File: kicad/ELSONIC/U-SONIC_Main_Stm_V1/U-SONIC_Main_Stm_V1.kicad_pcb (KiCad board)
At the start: 2 copper layers, 200 x 150 mm, 193 parts, among them IC1 LM5005MHX_NOPB, J1 SMW250-02P, J2 Screw_Terminal_01x06, J3 ARM_SWD_10, J4 Conn_01x06_HEADERPIN, J5 Conn_01x03, J6 Conn_02x10_Odd_Even, J7 SMW250-02P, J8 Conn_02x13_Odd_Even, K1 G6A274, K2 PA1A_5V, K3 PA1A_5V, K4 G6A274, K5 PA1A_5V, K6 G6A274, K7 PA1A_5V, K8 PA1A_5V, K9 G6A274, Q1 STD25N10F7, Q2 STD25N10F7, SW1 TS-1088, SW2 DSHP02T, T1 TOROID_OUTPUT_OD20_T6T12, T2 TOROID_CT_OD16_T1T20, U1 AMS1117-3.3, U10 TLP185GB-S, U11 TLP185GB-S, U12 TLP185GB-S, U2 UCC21520DWR, U3 STM32G474RBT6, U4 INA190A3IDCKR, U5 MAX3485ESA, U6 TLP185GB-S, U7 ULN2003ADR, U8 ULN2003ADR, U9 TLP185GB-S, Y1 X49SM8M

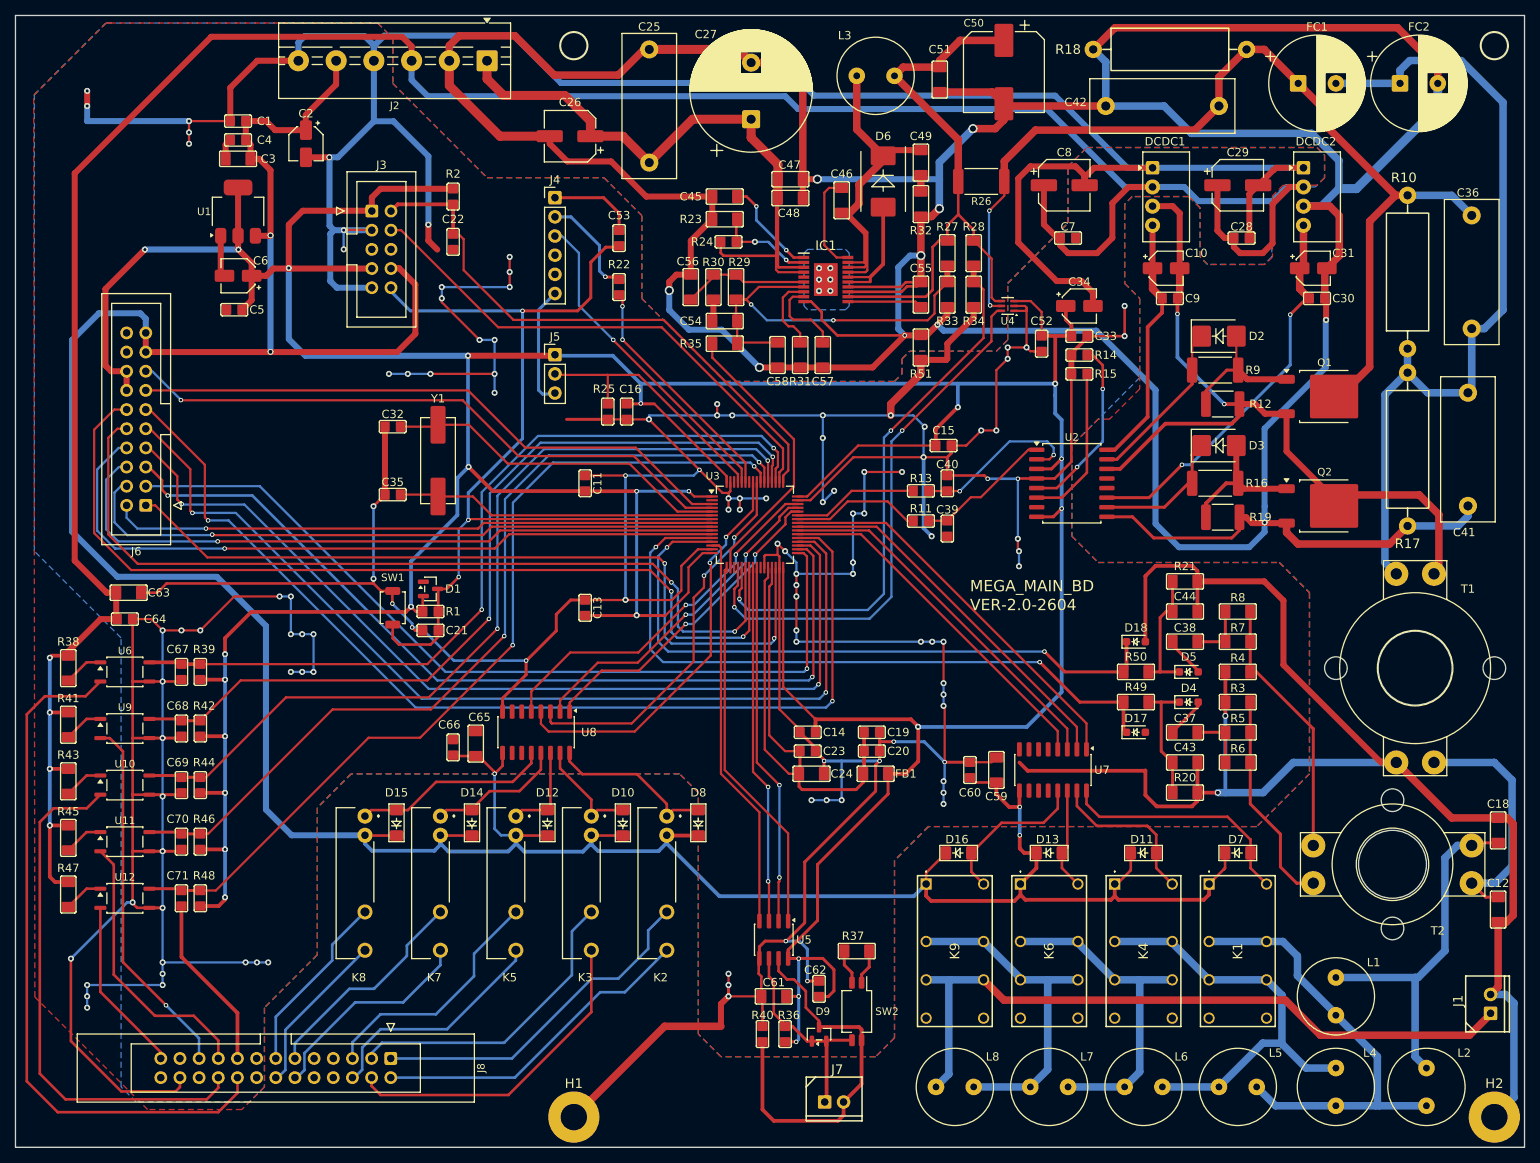
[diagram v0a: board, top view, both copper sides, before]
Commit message: feat: update ultrasonic controller and board design
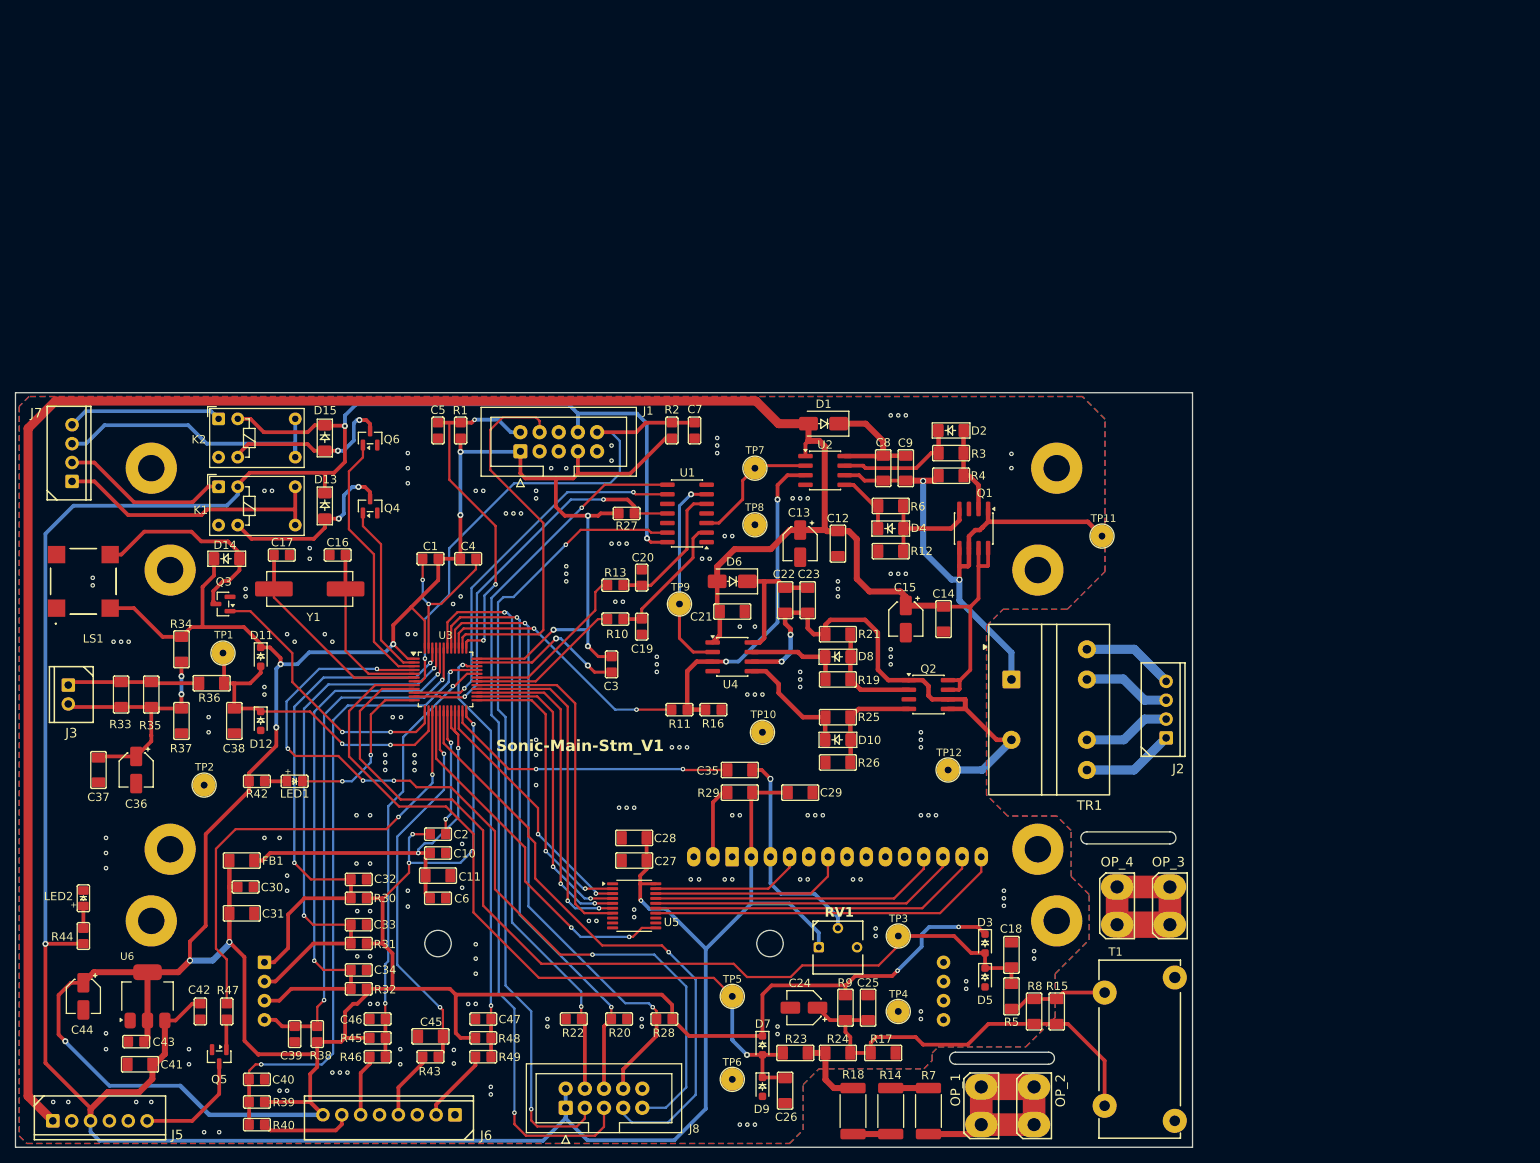
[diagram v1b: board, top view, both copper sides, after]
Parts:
- removed C48: CL31B225K, 04_MyFoot_Passive:C_3216Metric
- removed C49, C57: 1206CG331J101NT, 04_MyFoot_Passive:C_3216Metric
- removed C50: 220UF50V67RV, 04_MyFoot_Passive:CP_Elec_10x10.5
- removed C51: CL31A106K, 04_MyFoot_Passive:C_3216Metric
- removed C52, C53, C60, C62, C64, C66: CL21B104K, 04_MyFoot_Passive:C_2012Metric
- removed C54, C58: 1206B103K, 04_MyFoot_Passive:C_3216Metric
- removed C55: 1206CG102J101NT, 04_MyFoot_Passive:C_3216Metric
- removed C56: 1206CG101J, 04_MyFoot_Passive:C_3216Metric
- removed C59, C65: CL31B106K, 04_MyFoot_Passive:C_3216Metric
- removed C61, C63: CL31B105K, 04_MyFoot_Passive:C_3216Metric
- removed C67, C68, C69, C70, C71: CL21B472K, 04_MyFoot_Passive:C_2012Metric
- removed D16: LL4148, 03_MyFoot_Active:LL4148_MELF
- removed D17, D18: MM3Z3V6, 03_MyFoot_Active:D_SOD-323_HandSoldering
- removed DCDC1, DCDC2: MUS2415N, 05_MyFoot_Others:MUS2415N
- removed FC1, FC2: 470UF63V, 04_MyFoot_Passive:CP_Radial_D12.5mm_P5.00mm
- removed IC1: LM5005MHX_NOPB, 01_MyFoot_ICs:SOP65P640X110-21N
- removed K3, K5, K7, K8: PA1A_5V, 06_MyFoot_Mechanical:PA1A5V
- removed K4, K6, K9: G6A274, 06_MyFoot_Mechanical:G6A274PST15USDC12
- removed L1: 3.3uH, 04_MyFoot_Passive:L_Radial_D10.0mm_P5.00mm
- removed L2: 3.9uH, 04_MyFoot_Passive:L_Radial_D10.0mm_P5.00mm
- removed L3: 33uH, 04_MyFoot_Passive:L_Radial_D10.0mm_P5.00mm
- removed L4: 1.5uH, 04_MyFoot_Passive:L_Radial_D10.0mm_P5.00mm
- removed L5: 2.2uH, 04_MyFoot_Passive:L_Radial_D10.0mm_P5.00mm
- removed L6: 2.7uH, 04_MyFoot_Passive:L_Radial_D10.0mm_P5.00mm
- removed L7: 4.7uH, 04_MyFoot_Passive:L_Radial_D10.0mm_P5.00mm
- removed L8: 6.8uH, 04_MyFoot_Passive:L_Radial_D10.0mm_P5.00mm
- removed R41: W4J0472, 04_MyFoot_Passive:R_3216Metric
- removed R50: W4J0102, 04_MyFoot_Passive:R_3216Metric
- removed R51: W4F0000, 04_MyFoot_Passive:R_3216Metric
- removed SW1: TS-1088, 06_MyFoot_Mechanical:SW_SPST_TS-1088-xR025
- removed SW2: DSHP02T, 06_MyFoot_Mechanical:CHS-02B_W7.62mm_P1.27mm
- removed T2: TOROID_CT_OD16_T1T20, 04_MyFoot_Passive:Toroid_OD16mm_ID9.6-T1T20
- removed U10, U11, U12, U9: TLP185GB-S, 01_MyFoot_ICs:SOIC-4_4.55x3.7mm_P2.54mm
- removed U7, U8: ULN2003ADR, 01_MyFoot_ICs:SOIC-16_3.9x9.9mm_P1.27mm
- added C17: CG330J, 04_MyFoot_Passive:C_2012Metric, F.Cu at (35.3, -78.5)
- added LCD1: LC1622, 06_MyFoot_Mechanical:LC1622_1, B.Cu at (78.0, -60.0)
- added LED1: LED_SMD_KT_0805R, 03_MyFoot_Active:LED_2012Metric, F.Cu at (37.0, -48.5)
- added LED2: LED_SMD_KT_0805R, 03_MyFoot_Active:LED_2012Metric, F.Cu at (9.00, -33.0)
- added LS1: MLT-8530, 03_MyFoot_Active:MLT8530, F.Cu at (9.00, -75.0)
- added OP_1: TAP_250, 02_MyFoot_Connectors:TAP_250, F.Cu at (128.0, -5.50)
- added OP_2: TAP_250, 02_MyFoot_Connectors:TAP_250, F.Cu at (135.0, -5.50)
- added OP_3: TAP_250, 02_MyFoot_Connectors:TAP_250, F.Cu at (153.0, -32.0)
- added OP_4: TAP_250, 02_MyFoot_Connectors:TAP_250, F.Cu at (146.0, -32.0)
- added Q3: KRC105S, 03_MyFoot_Active:SOT-23_KRC105S, F.Cu at (27.5, -72.0)
- added Q4: KRC105S, 03_MyFoot_Active:SOT-23_KRC105S, F.Cu at (47.0, -85.0)
- added Q5: 2SC5343, 03_MyFoot_Active:SOT-23, F.Cu at (27.0, -12.0)
- added Q6: KRC105S, 03_MyFoot_Active:SOT-23_KRC105S, F.Cu at (47.0, -94.0)
- added RV1: 3362P103, 04_MyFoot_Passive:TRIM_3362P, F.Cu at (109.0, -26.5)
- added TP1: TPOINT, 05_MyFoot_Others:TP, F.Cu at (27.5, -65.5)
- added TP10: TPOINT, 05_MyFoot_Others:TP, F.Cu at (99.0, -55.0)
- added TP11: TPOINT, 05_MyFoot_Others:TP, F.Cu at (144.0, -81.0)
- added TP12: TPOINT, 05_MyFoot_Others:TP, F.Cu at (123.6, -50.0)
- added TP2: TPOINT, 05_MyFoot_Others:TP, F.Cu at (25.0, -48.0)
- added TP3: TPOINT, 05_MyFoot_Others:TP, F.Cu at (117.0, -28.0)
- added TP4: TPOINT, 05_MyFoot_Others:TP, F.Cu at (117.0, -18.0)
- added TP5: TPOINT, 05_MyFoot_Others:TP, F.Cu at (95.0, -20.0)
- added TP6: TPOINT, 05_MyFoot_Others:TP, F.Cu at (95.0, -9.00)
- added TP7: TPOINT, 05_MyFoot_Others:TP, F.Cu at (98.0, -90.0)
- added TP8: TPOINT, 05_MyFoot_Others:TP, F.Cu at (98.0, -82.5)
- added TP9: TPOINT, 05_MyFoot_Others:TP, F.Cu at (88.0, -72.0)
- added TR1: EI2218, 04_MyFoot_Passive:EI2218, F.Cu at (137.0, -58.0)
- C10, C2, C34, C6: value 10UF25V67RV -> CL21B104K; footprint 04_MyFoot_Passive:CP_Elec_4x5.4 -> 04_MyFoot_Passive:C_2012Metric
- C11, C28: value CL21B104K -> CL31B475K; footprint 04_MyFoot_Passive:C_2012Metric -> 04_MyFoot_Passive:C_3216Metric
- C12: value CG100J -> CL31B105K
- C13, C15: value CL21B104K -> 10UF25V67RV; footprint 04_MyFoot_Passive:C_2012Metric -> 04_MyFoot_Passive:CP_Elec_4x5.4
- C14, C21: value CL21B104K -> CL31B105K; footprint 04_MyFoot_Passive:C_2012Metric -> 04_MyFoot_Passive:C_3216Metric
- C16: value CL21B104K -> CG330J
- C18: value CG100J -> 22pF
- C19: value CL21B104K -> CG220J
- C20: value CL21B475K -> CG220J
- C22: value CL21C101J -> CL31B105K; footprint 04_MyFoot_Passive:C_2012Metric -> 04_MyFoot_Passive:C_3216Metric
- C23, C9: value CL21B104K -> CL31B104K; footprint 04_MyFoot_Passive:C_2012Metric -> 04_MyFoot_Passive:C_3216Metric
- C24: value CL31B106K -> 10UF25V67RV; footprint 04_MyFoot_Passive:C_3216Metric -> 04_MyFoot_Passive:CP_Elec_4x5.4
- C25: value 0.1uF100V -> CL31B104K; footprint 04_MyFoot_Passive:C_Rect_W7.0mm_P15.00mm -> 04_MyFoot_Passive:C_3216Metric
- C26: value 10UF100V67RV -> 22pF; footprint 04_MyFoot_Passive:CP_Elec_6.3x7.7 -> 04_MyFoot_Passive:C_3216Metric
- C27: value 1000UF63V -> CL31B104K; footprint 04_MyFoot_Passive:CP_Radial_D16.0mm_P7.50mm -> 04_MyFoot_Passive:C_3216Metric
- C29: value 47UF50V67RV -> CL31B104K; footprint 04_MyFoot_Passive:CP_Elec_6.3x7.7 -> 04_MyFoot_Passive:C_3216Metric
- C3: value CL31B106K -> CL21B104K; footprint 04_MyFoot_Passive:C_3216Metric -> 04_MyFoot_Passive:C_2012Metric
- C31: value 10UF25V67RV -> CL31B475K; footprint 04_MyFoot_Passive:CP_Elec_4x5.4 -> 04_MyFoot_Passive:C_3216Metric
- C32: value CG330J -> CL21B104K
- C35: value CG330J -> CL31B104K; footprint 04_MyFoot_Passive:C_2012Metric -> 04_MyFoot_Passive:C_3216Metric
- C36: value 0.1uF100V -> 10UF25V67RV; footprint 04_MyFoot_Passive:C_Rect_W7.0mm_P15.00mm -> 04_MyFoot_Passive:CP_Elec_4x5.4
- C39, C40: value CG220J -> CL21B104K
- C41: value 0.1uF100V -> CL31B106K; footprint 04_MyFoot_Passive:C_Rect_W7.0mm_P15.00mm -> 04_MyFoot_Passive:C_3216Metric
- C42: value 1uF100V -> CL21B104K; footprint 04_MyFoot_Passive:C_Rect_W7.0mm_P15.00mm -> 04_MyFoot_Passive:C_2012Metric
- C43: value CL31B104K -> CL21B104K; footprint 04_MyFoot_Passive:C_3216Metric -> 04_MyFoot_Passive:C_2012Metric
- C44: value CL31B104K -> 10UF25V67RV; footprint 04_MyFoot_Passive:C_3216Metric -> 04_MyFoot_Passive:CP_Elec_4x5.4
- C45: value 1206B105K101NT -> CL31B105K
- C46: value 1206B223K101NT -> CL21B104K; footprint 04_MyFoot_Passive:C_3216Metric -> 04_MyFoot_Passive:C_2012Metric
- C47: value CL31B225K -> CL21B104K; footprint 04_MyFoot_Passive:C_3216Metric -> 04_MyFoot_Passive:C_2012Metric
- C5: value CL21B104K -> CL21C101J
- C8: value 47UF50V67RV -> CL31B105K; footprint 04_MyFoot_Passive:CP_Elec_6.3x7.7 -> 04_MyFoot_Passive:C_3216Metric
- D1: value BAV99 -> UF4007; footprint 03_MyFoot_Active:SOT-23 -> 03_MyFoot_Active:D_SMA
- D11, D12, D7: value LL4148 -> BAT54WSQ-7; footprint 03_MyFoot_Active:LL4148_MELF -> 03_MyFoot_Active:D_SOD-323_HandSoldering
- D2: value SS24B -> LL4148; footprint 03_MyFoot_Active:D_SMB -> 03_MyFoot_Active:LL4148_MELF
- D3: value SS24B -> BAT54WSQ-7; footprint 03_MyFoot_Active:D_SMB -> 03_MyFoot_Active:D_SOD-323_HandSoldering
- D4: value BAT54WSQ-7 -> LL4148; footprint 03_MyFoot_Active:D_SOD-323_HandSoldering -> 03_MyFoot_Active:LL4148_MELF
- D6: value B3100-13-F -> UF4007; footprint 03_MyFoot_Active:B3100_13_F -> 03_MyFoot_Active:D_SMA
- D9: value SM712-LF-T7 -> BAT54WSQ-7; footprint Package_TO_SOT_SMD:SOT-23 -> 03_MyFoot_Active:D_SOD-323_HandSoldering
- H3, H4: value MountingHole -> MountingHole_Pad; footprint 06_MyFoot_Mechanical:MTHole_3.5mm -> 06_MyFoot_Mechanical:MTHole_3.5mm_6.8mmPad_GND
- J1: value SMW250-02P -> ARM_SWD_10; footprint 02_MyFoot_Connectors:SMW250_02P -> 02_MyFoot_Connectors:IDC-Header_2x05_P2.54mm_Vertical
- J2: value Screw_Terminal_01x06 -> SMW250-04P; footprint 02_MyFoot_Connectors:TB_P5.00mm_6P -> 02_MyFoot_Connectors:SMW250_04P
- J3: value ARM_SWD_10 -> SMW250-02P; footprint 02_MyFoot_Connectors:IDC-Header_2x05_P2.54mm_Vertical -> 02_MyFoot_Connectors:SMW250_02P
- J4: value Conn_01x06_HEADERPIN -> SW_BD; footprint 02_MyFoot_Connectors:PinHeader_1x06_P2.54mm_Vertical -> 05_MyFoot_Others:SW_BD; moved to B.Cu
- J5: value Conn_01x03 -> SMW250-06P; footprint 02_MyFoot_Connectors:PinHeader_1x03_P2.54mm_Vertical -> 02_MyFoot_Connectors:SMW250_06P
- J6: value Conn_02x10_Odd_Even -> SMW250-08P; footprint 02_MyFoot_Connectors:IDC-Header_2x10_P2.54mm_Vertical -> 02_MyFoot_Connectors:SMW250_08P
- J7: value SMW250-02P -> SMW250-04P; footprint 02_MyFoot_Connectors:SMW250_02P -> 02_MyFoot_Connectors:SMW250_04P
- J8: value Conn_02x13_Odd_Even -> RS485_BD; footprint 02_MyFoot_Connectors:IDC-Header_2x13_P2.54mm_Latch_Vertical -> 02_MyFoot_Connectors:IDC-Header_2x05_P2.54mm_Vertical
- K1: value G6A274 -> HR92; footprint 06_MyFoot_Mechanical:G6A274PST15USDC12 -> 06_MyFoot_Mechanical:Relay_SPDT_HsinDa_Y14
- K2: value PA1A_5V -> HR92; footprint 06_MyFoot_Mechanical:PA1A5V -> 06_MyFoot_Mechanical:Relay_SPDT_HsinDa_Y14
- Q1, Q2: value STD25N10F7 -> IRF7351; footprint Package_TO_SOT_SMD:TO-252-2 -> 01_MyFoot_ICs:SOIC-8_3.9x4.9mm_P1.27mm
- R10: value 15K/3W -> 0805FR-0747RL; footprint 04_MyFoot_Passive:R_Axial_2W_P20.32mm -> 04_MyFoot_Passive:R_2012Metric
- R11: value 0805FR-0747RL -> WR08X1000FTL
- R12: value 1812J103 -> RS-06K103JT; footprint 04_MyFoot_Passive:R_4532Metric -> 04_MyFoot_Passive:R_3216Metric
- R14: value W8J0103 -> 100K/1W; footprint 04_MyFoot_Passive:R_2012Metric -> 04_MyFoot_Passive:R_6332Metric
- R15: value 0805FR-07100K -> FRC1206F2400TS; footprint 04_MyFoot_Passive:R_2012Metric -> 04_MyFoot_Passive:R_3216Metric
- R16: value 25121WF470 -> WR08X1002FTL; footprint 04_MyFoot_Passive:R_6332Metric -> 04_MyFoot_Passive:R_2012Metric
- R17: value 15K/3W -> 10K; footprint 04_MyFoot_Passive:R_Axial_2W_P20.32mm -> 04_MyFoot_Passive:R_3216Metric
- R18: value 22K/3W -> 100K/1W; footprint 04_MyFoot_Passive:R_Axial_2W_P20.32mm -> 04_MyFoot_Passive:R_6332Metric
- R19: value 1812J103 -> RS-06K22R; footprint 04_MyFoot_Passive:R_4532Metric -> 04_MyFoot_Passive:R_3216Metric
- R20: value W4F1002 -> WR08X1002FTL; footprint 04_MyFoot_Passive:R_3216Metric -> 04_MyFoot_Passive:R_2012Metric
- R21: value W4F1002 -> RS-06K103JT
- R22: value 0805FR-0733RL -> WR08X1002FTL
- R23: value W4J0123 -> 1K
- R24: value W4J0334 -> 1K; footprint 04_MyFoot_Passive:R_2012Metric -> 04_MyFoot_Passive:R_3216Metric
- R25: value W8J0103 -> RS-06K22R; footprint 04_MyFoot_Passive:R_2012Metric -> 04_MyFoot_Passive:R_3216Metric
- R26: value FRL2512FR047TS-47mohm -> RS-06K103JT; footprint 04_MyFoot_Passive:R_2512_6332Metric -> 04_MyFoot_Passive:R_3216Metric
- R27: value W4F7502 -> RS-05K472JT; footprint 04_MyFoot_Passive:R_3216Metric -> 04_MyFoot_Passive:R_2012Metric
- R28: value W4F9102 -> WR08X1002FTL; footprint 04_MyFoot_Passive:R_3216Metric -> 04_MyFoot_Passive:R_2012Metric
- R29: value W4J0223 -> RS-06K47R
- R3: value AR06CTC0500 -> RS-06K22R
- R30: value W4F4992 -> W8J0103; footprint 04_MyFoot_Passive:R_3216Metric -> 04_MyFoot_Passive:R_2012Metric
- R31: value W4J0333 -> W8J0103; footprint 04_MyFoot_Passive:R_3216Metric -> 04_MyFoot_Passive:R_2012Metric
- R32: value W4J0100 -> W8J0103; footprint 04_MyFoot_Passive:R_3216Metric -> 04_MyFoot_Passive:R_2012Metric
- R33: value W4F4991 -> FRC1206F2400TS
- R34: value W4F1002 -> 10K
- R35: value W4F8871 -> FRC1206F2400TS
- R36: value W8J0431 -> 1K; footprint 04_MyFoot_Passive:R_2012Metric -> 04_MyFoot_Passive:R_3216Metric
- R37: value W4J0121 -> 10K
- R38, R45: value W4J0472 -> W8J0103; footprint 04_MyFoot_Passive:R_3216Metric -> 04_MyFoot_Passive:R_2012Metric
- R4: value AR06CTC0500 -> RS-06K103JT
- R40: value W8J0431 -> RS-05K470JT
- R42, R44: value W8J0103 -> 0805W8J0202T5E
- R43: value W4J0472 -> 0805W8F1000T; footprint 04_MyFoot_Passive:R_3216Metric -> 04_MyFoot_Passive:R_2012Metric
- R46: value W8J0103 -> RS-05K470JT
- R47: value W4J0472 -> RS-05K471JT; footprint 04_MyFoot_Passive:R_3216Metric -> 04_MyFoot_Passive:R_2012Metric
- R49: value W4J0102 -> RS-05K470JT; footprint 04_MyFoot_Passive:R_3216Metric -> 04_MyFoot_Passive:R_2012Metric
- R5: value W4F4700 -> 1K
- R6: value W4F4700 -> RS-06K22R
- R7: value W4F4700 -> 100K/1W; footprint 04_MyFoot_Passive:R_3216Metric -> 04_MyFoot_Passive:R_6332Metric
- R8: value W4F4700 -> FRC1206F2400TS
- R9: value 25121WF470 -> 10K; footprint 04_MyFoot_Passive:R_6332Metric -> 04_MyFoot_Passive:R_3216Metric
- T1: value TOROID_OUTPUT_OD20_T6T12 -> SCT-17P; footprint 04_MyFoot_Passive:Toroid_OD20mm_ID10-T6T12 -> 04_MyFoot_Passive:SCT-17P
- U1: value AMS1117-3.3 -> 74AHCT125; footprint 01_MyFoot_ICs:SOT-223-3_TabPin2 -> 01_MyFoot_ICs:SOIC-14_3.9x8.7mm_P1.27mm
- U2: value UCC21520DWR -> IR2104; footprint 01_MyFoot_ICs:SOIC-16W_7.5x10.3mm_P1.27mm -> 01_MyFoot_ICs:SOIC-8_3.9x4.9mm_P1.27mm
- U3: value STM32G474RBT6 -> STM32G474CBT6; footprint Package_QFP:LQFP-64_10x10mm_P0.5mm -> Package_QFP:LQFP-48_7x7mm_P0.5mm
- U4: value INA190A3IDCKR -> IR2104; footprint Package_TO_SOT_SMD:SOT-363_SC-70-6 -> 01_MyFoot_ICs:SOIC-8_3.9x4.9mm_P1.27mm
- U5: value MAX3485ESA -> 74HCT574PWR; footprint 01_MyFoot_ICs:SOIC-8_3.9x4.9mm_P1.27mm -> 01_MyFoot_ICs:TSSOP-20_4.4x6.5mm_P0.65mm
- U6: value TLP185GB-S -> AMS1117-3.3; footprint 01_MyFoot_ICs:SOIC-4_4.55x3.7mm_P2.54mm -> 01_MyFoot_ICs:SOT-223-3_TabPin2
- moved C41 194.0 mm to (16.5, -11.0), turned to 0 degrees
- moved C36 188.9 mm to (16.0, -50.0), turned to -90 degrees
- moved H2 179.9 mm to (18.0, -30.0)
- moved C42 175.1 mm to (24.5, -18.0), turned to 90 degrees
- moved C31 165.8 mm to (30.0, -31.0), turned to 180 degrees
- moved C30 162.0 mm to (30.5, -34.5)
- moved C44 154.7 mm to (9.00, -20.0), turned to -90 degrees
- moved R18 146.8 mm to (111.0, -4.80), turned to -90 degrees
- moved J1 144.2 mm to (72.0, -93.5)
- moved C37 144.1 mm to (11.0, -50.0), turned to 90 degrees
- moved C43 143.8 mm to (16.0, -14.0), turned to 0 degrees
- moved K1 135.8 mm to (32.0, -85.0), turned to 0 degrees
- moved J2 133.8 mm to (152.5, -58.0), turned to 90 degrees
- moved J7 132.7 mm to (7.50, -92.0), turned to 90 degrees
- moved H3 132.5 mm to (138.0, -30.0)
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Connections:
- C1 pad 2: +5V -> +3.3V
- C10 pad 1: +15VA -> GND
- C10 pad 2: GNDA -> Net-(U3-VDDA)
- C11 pad 2: +3.3V -> Net-(U3-VDDA)
- C12 pad 2: Net-(C12-Pad2) -> +12V
- C13 pad 1: GND -> +12V
- C13 pad 2: +3.3V -> GND
- C14 pad 2: +3.3V -> +12V
- C15 pad 1: GND -> +12V
- C15 pad 2: +3.3V -> GND
- C16 pad 2: +3.3V -> Net-(U3-PF0)
- C18 pad 2: Net-(C18-Pad2) -> /ADC1_IN2_COMP1
- C19 pad 2: Net-(U3-VDDA) -> /INA
- C2 pad 1: +5V -> GND
- C2 pad 2: GND -> +3.3V
- C20 pad 2: Net-(U3-VDDA) -> /INB
- C21 pad 2: /NRST -> +12V
- C22 pad 1: GND -> Net-(Q2A-S1)
- C22 pad 2: /SWDIO -> Net-(D6-K)
- C23 pad 1: GND -> Net-(Q2A-S1)
- C23 pad 2: Net-(U3-VDDA) -> Net-(D6-K)
- C24 pad 1: GND -> Net-(C24-Pad1)
- C24 pad 2: Net-(U3-VDDA) -> GND
- C25 pad 1: GNDB -> GND
- C25 pad 2: +48V -> Net-(C24-Pad1)
- C26 pad 1: +48V -> GND
- C26 pad 2: GNDB -> /ADC1_IN1_COMP3
- C27 pad 1: +48V -> GND
- C27 pad 2: GNDB -> +5V
- C28 pad 2: +24V -> +5V
- C29 pad 1: +24V -> GND
- C29 pad 2: GND -> +5V
- C3 pad 2: +5V -> +3.3V
- C30 pad 1: GNDB -> GND
- C30 pad 2: +15VB -> +3.3V
- C31 pad 1: +15VB -> GND
- C31 pad 2: GNDB -> +3.3V
- C32 pad 1: GND -> /START_STOP
- C32 pad 2: Net-(U3-PF0) -> GND
- C33 pad 1: GND -> /UP
- C33 pad 2: +3.3V -> GND
- C34 pad 1: +3.3V -> /DOWN
- C35 pad 2: Net-(U3-PF1) -> Net-(LCD1-VO)
- C36 pad 2: +VBUS -> GND
- C37 pad 1: Net-(D4-A) -> GND
- C37 pad 2: Net-(C37-Pad2) -> Net-(C36-Pad1)
- C38 pad 1: Net-(D5-A) -> GND
- C38 pad 2: Net-(C38-Pad2) -> /ADC2_IN3
- C39 pad 1: GND -> /MODE
- C39 pad 2: /INA -> GND
- C4 pad 2: +5V -> +3.3V
- C40 pad 1: GND -> /RUN_SW
- C40 pad 2: /INB -> GND
- C41 pad 1: GNDB -> GND
- C41 pad 2: Net-(C36-Pad1) -> +5V
- C42 pad 1: GNDB -> GND
- C42 pad 2: +VBUS -> +5V
- C43 pad 2: Net-(D4-K) -> +3.3V
- C44 pad 1: GND -> +3.3V
- C44 pad 2: Net-(D5-K) -> GND
- C45 pad 1: GNDB -> GND
- C45 pad 2: Net-(IC1-VCC) -> /PWM_VR
- C46 pad 1: Net-(D6-K) -> /REMOTE
- C46 pad 2: Net-(IC1-BST) -> GND
- C47 pad 1: GNDB -> /SWEEP_SW
- C47 pad 2: +48V -> GND
- C5 pad 2: +3.3V -> /SWDIO
- C6 pad 1: +3.3V -> GND
- C6 pad 2: GND -> Net-(U3-VDDA)
- C7 pad 2: +24V -> /NRST
- C8 pad 1: +24V -> Net-(Q1A-S1)
- C8 pad 2: GND -> Net-(D1-K)
- C9 pad 1: GNDA -> Net-(Q1A-S1)
- C9 pad 2: +15VA -> Net-(D1-K)
- D1 pad 1: GND -> Net-(D1-K)
- D1 pad 2: +3.3V -> +12V
- D10 pad 1: +5V -> Net-(D10-K)
- D11 pad 1: +5V -> +3.3V
- D11 pad 2: Net-(D11-A) -> /ADC2_IN3
- D12 pad 1: +5V -> /ADC2_IN3
- D12 pad 2: Net-(D12-A) -> GND
- D14 pad 1: +5V -> +3.3V
- D2 pad 1: Net-(D2-A1) -> Net-(D2-K)
- D2 pad 2: Net-(D2-A2) -> Net-(D2-A)
- D3 pad 1: Net-(D3-A1) -> +3.3V
- D3 pad 2: Net-(D3-A2) -> /ADC1_IN2_COMP1
- D5 pad 1: Net-(D5-K) -> /ADC1_IN2_COMP1
- D5 pad 2: Net-(D5-A) -> GND
- D6 pad 2: Net-(D6-A) -> +12V
- D7 pad 1: +5V -> +3.3V
- D7 pad 2: Net-(D7-A) -> /ADC1_IN1_COMP3
- D8 pad 1: +5V -> Net-(D8-K)
- D9 pad 1: Net-(D9-A1) -> /ADC1_IN1_COMP3
- D9 pad 2: Net-(D9-A1) -> GND
- J1 pad 1: /LC_RELAY_OUT -> +3.3V
- J1 pad 2: GND -> /SWDIO
- J2 pad 1: +48V -> Net-(J2-Pad1)
- J2 pad 2: GNDB -> Net-(J2-Pad2)
- J2 pad 3: +24V -> Net-(J2-Pad3)
- J2 pad 4: GND -> Net-(J2-Pad4)
- J3 pad 1: +3.3V -> Net-(J3-Pad1)
- J3 pad 2: /SWDIO -> Net-(C36-Pad1)
- J4 pad 1: /DTR -> /START_STOP
- J4 pad 2: /USART1_TX -> /UP
- J4 pad 3: /USART1_RX -> /DOWN
- J4 pad 4: unconnected-(J4-Pin_4-Pad4) -> /MODE
- J4 pad 5: unconnected-(J4-Pin_5-Pad5) -> GND
- J5 pad 1: +3.3V -> +12V
- J5 pad 2: Net-(J5-Pin_2) -> GND
- J5 pad 3: GND -> +5V
- J6 pad 1: /D0 -> GND
- J6 pad 2: /START_STOP -> Net-(J6-Pad2)
- J6 pad 3: /D1 -> GND
- J6 pad 4: /MODE -> Net-(J6-Pad4)
- J6 pad 5: /D2 -> GND
- J6 pad 6: /UP -> Net-(J6-Pad6)
- J6 pad 7: /D3 -> Net-(J6-Pad7)
- J6 pad 8: /DOWN -> +3.3V
- J7 pad 1: Net-(D9-A1) -> Net-(J7-Pad1)
- J7 pad 2: Net-(D9-common) -> Net-(J7-Pad2)
- J8 pad 1: /LOW_ALARM_A -> +5V
- J8 pad 10: unconnected-(J8-Pin_10-Pad10) -> GND
- J8 pad 2: /LOW_ALARM_C -> +5V
- J8 pad 3: /GOING_A -> /MAX485_RX
- J8 pad 4: /GOING_C -> //RE_RS485
- J8 pad 5: /HIGH_ALARM_A -> /MAX485_TX
- J8 pad 6: /HIGH_ALARM_C -> /DE_RS485
- J8 pad 7: unconnected-(J8-Pin_7-Pad7) -> /RTERM
- J8 pad 8: unconnected-(J8-Pin_8-Pad8) -> /485BD_DETECT
- J8 pad 9: unconnected-(J8-Pin_9-Pad9) -> /SPARE
- K1 pad 1: +5V -> Net-(J7-Pad2)
- K1 pad 4: /LC_RELAY_IN -> Net-(D13-A)
- K1 pad 6: Net-(K1-NC1) -> Net-(J7-Pad1)
- K2 pad 1: Net-(D8-A) -> Net-(J7-Pad4)
- K2 pad 2: +5V -> unconnected-(K2-Pad2)
- K2 pad 5: /LOW_ALARM_A -> Net-(J7-Pad3)
- K2 pad 6: /LOW_ALARM_C -> Net-(J7-Pad3)
- Q1 pad 1: Net-(D2-A2) -> Net-(Q1A-S1)
- Q1 pad 2: +VBUS -> Net-(D2-A)
- Q1 pad 3: GNDA -> GND
- Q2 pad 1: Net-(D3-A2) -> Net-(Q2A-S1)
- Q2 pad 2: GNDA -> Net-(D8-A)
- Q2 pad 3: GNDB -> GND
- R1 pad 1: /NRST -> /SWDIO
- R10 pad 1: Net-(C36-Pad1) -> /CHA1
- R10 pad 2: +VBUS -> /INA
- R11 pad 1: /CHA1 -> /SONIC_ON
- R11 pad 2: /INA -> Net-(U2-~{SD})
- R12 pad 1: GNDA -> GND
- R12 pad 2: Net-(D2-A2) -> Net-(D4-A)
- R14 pad 1: GND -> Net-(R14-Pad1)
- R14 pad 2: Net-(U2-DIS) -> Net-(R14-Pad2)
- R15 pad 1: GND -> Net-(C24-Pad1)
- R15 pad 2: Net-(U2-DT) -> Net-(R15-Pad2)
- R16 pad 1: Net-(D3-A2) -> GND
- R16 pad 2: Net-(D3-A1) -> Net-(U2-~{SD})
- R17 pad 1: GNDB -> GND
- R17 pad 2: Net-(C36-Pad1) -> Net-(C24-Pad1)
- R18 pad 1: GNDB -> Net-(R18-Pad1)
- R18 pad 2: +VBUS -> Net-(R14-Pad1)
- R19 pad 1: GNDB -> Net-(D8-K)
- R19 pad 2: Net-(D3-A2) -> Net-(D8-A)
- R2 pad 1: /SWDIO -> /NRST
- R20 pad 2: Net-(D4-K) -> /DE_RS485
- R21 pad 1: GND -> Net-(Q2A-S1)
- R21 pad 2: Net-(D5-K) -> Net-(D8-A)
- R22 pad 1: Net-(U3-PB6) -> GND
- R22 pad 2: /USART1_TX -> //RE_RS485
- R23 pad 1: Net-(IC1-SD) -> Net-(R18-Pad1)
- R23 pad 2: GNDB -> /ADC1_IN1_COMP3
- R24 pad 1: +48V -> Net-(C24-Pad1)
- R24 pad 2: Net-(IC1-SD) -> Net-(R18-Pad1)
- R25 pad 1: GND -> Net-(D10-K)
- R25 pad 2: Net-(J5-Pin_2) -> Net-(D10-A)
- R26 pad 1: +VBUS -> GND
- R26 pad 2: Net-(IC1-OUT) -> Net-(D10-A)
- R27 pad 1: Net-(IC1-FB) -> /USART2_RX
- R27 pad 2: Net-(IC1-OUT) -> +3.3V
- R28 pad 1: /ADC2_IN4 -> /485BD_DETECT
- R28 pad 2: Net-(IC1-OUT) -> +3.3V
- R29 pad 1: Net-(IC1-FB) -> Net-(LCD1-LED(+))
- R29 pad 2: Net-(IC1-COMP) -> +5V
- R3 pad 1: GND -> Net-(D2-K)
- R3 pad 2: Net-(R3-Pad2) -> Net-(D2-A)
- R30 pad 1: Net-(C54-Pad2) -> /START_STOP
- R30 pad 2: Net-(IC1-COMP) -> +3.3V
- R31 pad 1: GNDB -> /UP
- R31 pad 2: Net-(IC1-RT) -> +3.3V
- R32 pad 1: GNDB -> /DOWN
- R32 pad 2: Net-(C49-Pad1) -> +3.3V
- R33 pad 1: GNDB -> Net-(C36-Pad1)
- R33 pad 2: Net-(IC1-FB) -> Net-(J3-Pad1)
- R34 pad 1: GND -> Net-(C36-Pad1)
- R34 pad 2: /ADC2_IN4 -> +3.3V
- R35 pad 1: Net-(IC1-FB) -> Net-(C36-Pad1)
- R35 pad 2: /DAC1_OUT1 -> Net-(J3-Pad1)
- R36 pad 1: Net-(D9-A1) -> /ADC2_IN3
- R36 pad 2: +3.3V -> Net-(J3-Pad1)
- R37 pad 1: Net-(R37-Pad1) -> GND
- R37 pad 2: Net-(R37-Pad2) -> Net-(C36-Pad1)
- R38 pad 1: Net-(R38-Pad1) -> /MODE
- R38 pad 2: +24V -> +3.3V
- R39 pad 1: /REMOTE_M -> /RUN_SW
- R4 pad 1: GND -> Net-(Q1A-S1)
- R4 pad 2: Net-(R4-Pad2) -> Net-(D2-A)
- R40 pad 1: GND -> /RUN_SW
- R40 pad 2: Net-(D9-common) -> Net-(J6-Pad7)
- R42 pad 1: /BCD_BIT1_M -> Net-(LED1-A)
- R43 pad 1: Net-(R43-Pad1) -> /PWM_VR
- R43 pad 2: +24V -> Net-(J6-Pad4)
- R44 pad 1: /BCD_BIT2_M -> Net-(LED2-A)
- R44 pad 2: +3.3V -> +5V
- R45 pad 1: Net-(R45-Pad1) -> /REMOTE
- R45 pad 2: +24V -> +3.3V
- R46 pad 1: /BCD_BIT3_M -> /REMOTE
- R46 pad 2: +3.3V -> Net-(J6-Pad6)
- R47 pad 2: +24V -> /PWM_OUTPUT
- R48 pad 1: /SENSOR_M -> /SWEEP_SW
- R49 pad 1: Net-(D4-K) -> /SWEEP_SW
- R49 pad 2: /ADC1_IN1 -> Net-(J6-Pad2)
- R5 pad 1: Net-(C37-Pad2) -> /ADC1_IN2_COMP1
- R5 pad 2: Net-(R3-Pad2) -> Net-(R15-Pad2)
- R6 pad 1: Net-(C37-Pad2) -> Net-(D4-K)
- R6 pad 2: Net-(R3-Pad2) -> Net-(D4-A)
- R7 pad 1: Net-(C38-Pad2) -> Net-(R14-Pad2)
- R7 pad 2: Net-(R4-Pad2) -> /50V_550V_15kHz_128kHz
- R8 pad 1: Net-(C38-Pad2) -> Net-(C24-Pad1)
- R8 pad 2: Net-(R4-Pad2) -> Net-(R15-Pad2)
- R9 pad 1: Net-(D2-A2) -> Net-(C24-Pad1)
- R9 pad 2: Net-(D2-A1) -> +3.3V
- T1 pad 1: GNDA -> unconnected-(T1-Pad1)
- T1 pad 2: Net-(C36-Pad1) -> unconnected-(T1-Pad2)
- T1 pad 3: Net-(C12-Pad2) -> Net-(R15-Pad2)
- T1 pad 4: GND -> Net-(C24-Pad1)
- U1 pad 2: +3.3V -> /INA
- U1 pad 3: +5V -> Net-(TP7-Pin_1)
- U2 pad 1: /INA -> +12V
- U2 pad 2: /INB -> Net-(TP7-Pin_1)
- U2 pad 3: +3.3V -> Net-(U2-~{SD})
- U2 pad 5: Net-(U2-DIS) -> Net-(D4-K)
- U2 pad 6: Net-(U2-DT) -> Net-(Q1A-S1)
- U2 pad 7: unconnected-(U2-NC-Pad7) -> Net-(D2-K)
- U2 pad 8: +3.3V -> Net-(D1-K)
- U3 pad 10: /UP -> /USART2_TX
- U3 pad 11: /DOWN -> /USART2_RX
- U3 pad 12: /ADC1_IN1 -> /RUN_LED
- U3 pad 13: /ADC1_IN2 -> /BZ_OUT
- U3 pad 14: /USART2_TX -> /ADC2_IN3
- U3 pad 15: GND -> /PWM_OUTPUT
- U3 pad 16: +3.3V -> /CLK_LCD
- U3 pad 17: /USART2_RX -> /PWM_VR
- U3 pad 18: /DAC1_OUT1 -> /RTERM
- U3 pad 19: unconnected-(U3-PA5-Pad19) -> GND
- U3 pad 2: unconnected-(U3-PC13-Pad2) -> /GOING
- U3 pad 20: /ADC2_IN3 -> Net-(U3-VDDA)
- U3 pad 21: /ADC2_IN4 -> Net-(U3-VDDA)
- U3 pad 22: /SET -> /LCD_RS
- U3 pad 23: /BZ_OUT -> GND
- U3 pad 24: /DE_RS485 -> +3.3V
- U3 pad 25: //RE_RS485 -> /LCD_E
- U3 pad 26: unconnected-(U3-PB2-Pad26) -> /LCD_D4
- U3 pad 27: GND -> /LCD_D5
- U3 pad 28: Net-(U3-VDDA) -> /LCD_D6
- U3 pad 29: Net-(U3-VDDA) -> /LCD_D7
- U3 pad 3: /CLK_LCD -> /END_BZ
- U3 pad 30: /D0 -> /CHA1
- U3 pad 31: GND -> /CHA2
- U3 pad 32: +3.3V -> /REMOTE
- U3 pad 33: /D1 -> /RUN_SW
- U3 pad 34: /D2 -> /SWEEP_SW
- U3 pad 35: /D3 -> GND
- U3 pad 36: /D4 -> +3.3V
- U3 pad 37: /D5 -> /SWDIO
- U3 pad 38: /LC_REL1 -> /SWCLK
- U3 pad 39: /LC_REL2 -> /SONIC_ON
- U3 pad 4: /CLK_LED -> /SPARE
- U3 pad 40: /LC_REL3 -> /485BD_DETECT
- U3 pad 41: /LC_REL4 -> /DE_RS485
- U3 pad 42: /CHA1 -> //RE_RS485
- U3 pad 43: /CHA2 -> /MODE
- U3 pad 44: /LOW_ALARM -> /DOWN
- U3 pad 45: /GOING -> /UP
- U3 pad 46: /TOTAL_ALARM -> /START_STOP
- U3 pad 8: /START_STOP -> /ADC1_IN1_COMP3
- U3 pad 9: /MODE -> /ADC1_IN2_COMP1
- U4 pad 1: GND -> +12V
- U4 pad 2: GND -> Net-(TP9-Pin_1)
- U4 pad 3: +3.3V -> Net-(U2-~{SD})
- U4 pad 4: Net-(IC1-OUT) -> GND
- U4 pad 5: +VBUS -> Net-(D10-K)
- U4 pad 6: /ADC2_IN3 -> Net-(Q2A-S1)
- U5 pad 1: /USART2_RX -> GND
- U5 pad 2: //RE_RS485 -> /LCD_E
- U5 pad 3: /DE_RS485 -> /LCD_RS
- U5 pad 4: /USART2_TX -> /LCD_D4
- U5 pad 5: GND -> /LCD_D5
- U5 pad 6: Net-(D9-A1) -> /LCD_D6
- U5 pad 7: Net-(D9-common) -> /LCD_D7
- U5 pad 8: +3.3V -> unconnected-(U5-D6-Pad8)
- U6 pad 1: Net-(R38-Pad1) -> GND
- U6 pad 3: /REMOTE -> +5V
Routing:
- net GND: track 1481.6 -> 98.9 mm, vias 121 -> 195
- net GNDB: track 596.2 -> 0.00 mm, vias 10 -> 0
- net +24V: track 349.5 -> 0.00 mm, vias 4 -> 0
- net +12V: track 0.00 -> 297.7 mm
- net /D5: track 136.9 -> 0.00 mm, vias 2 -> 0
- net +VBUS: track 132.6 -> 0.00 mm, vias 2 -> 0
- net /D4: track 131.4 -> 0.00 mm, vias 2 -> 0
- net /ADC1_IN2_COMP1: track 0.00 -> 127.2 mm
- net /D3: track 125.2 -> 0.00 mm, vias 2 -> 0
- net /D2: track 119.5 -> 0.00 mm, vias 2 -> 0
- net /SENSOR_M: track 117.5 -> 0.00 mm, vias 2 -> 0
- net /MAX485_TX: track 0.00 -> 116.0 mm, vias 0 -> 2
- net /SET: track 116.0 -> 0.00 mm, vias 2 -> 0
- net /SPARE: track 0.00 -> 115.8 mm, vias 0 -> 5
- net /BCD_BIT3_M: track 115.7 -> 0.00 mm, vias 2 -> 0
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- removed copper zone on B.Cu, net unconnected-(IC1-EP-Pad21)
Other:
- board size 200 x 150 mm -> 156 x 100 mm
- board text added: "Sonic-Main-Stm_V1"
- board text removed: "MEGA_MAIN_BD"
- board text removed: "VER-2.0-2604"
